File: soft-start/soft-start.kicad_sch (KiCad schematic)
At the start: 17 parts

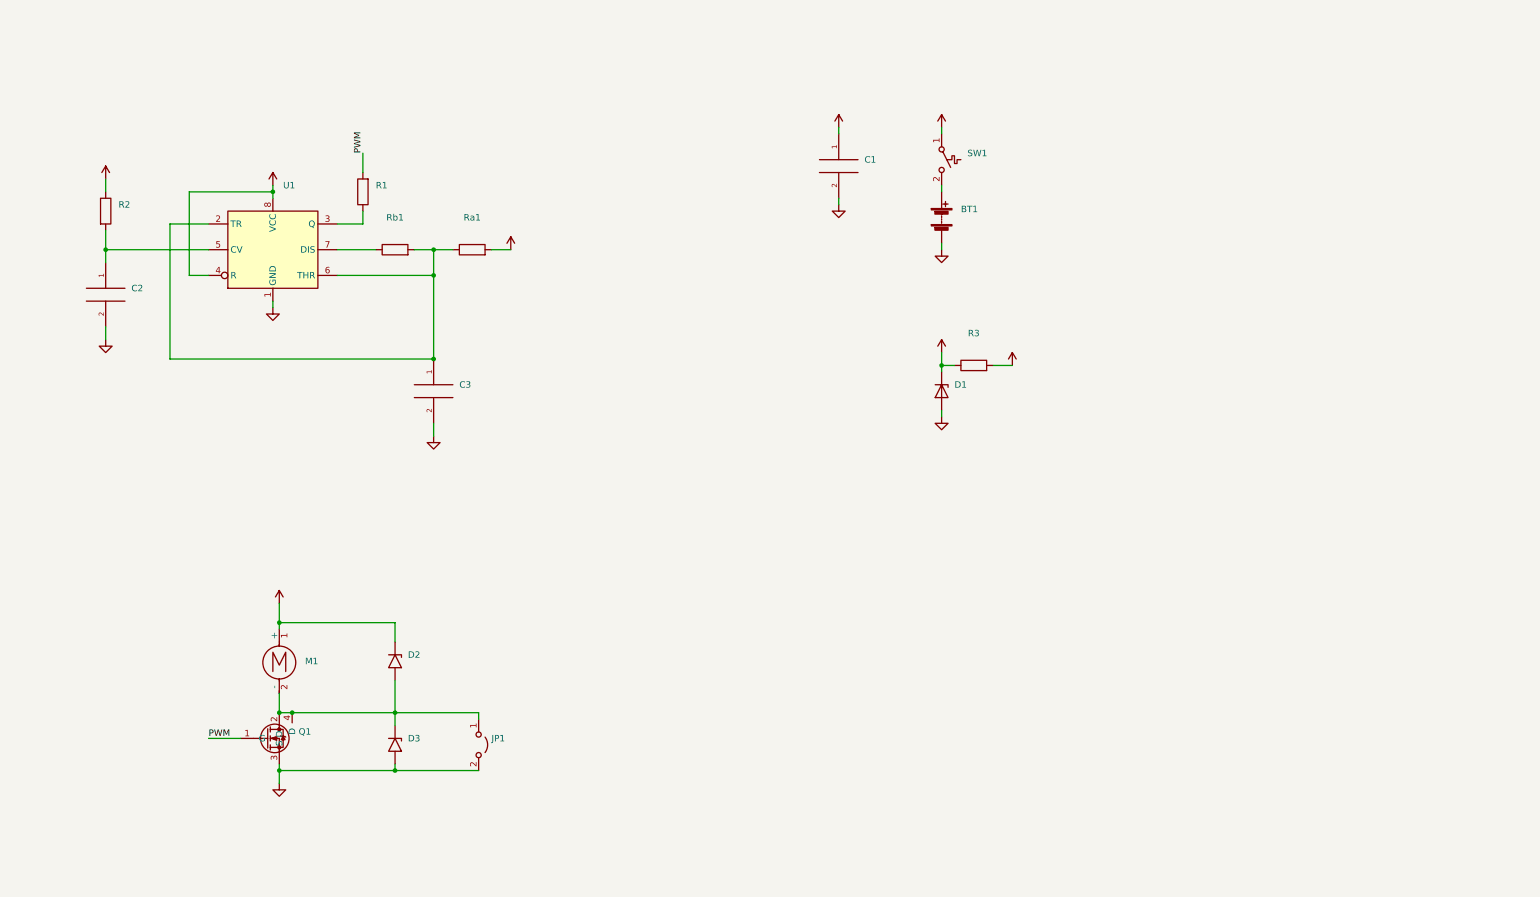
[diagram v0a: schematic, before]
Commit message: [soft-start] Add power supply
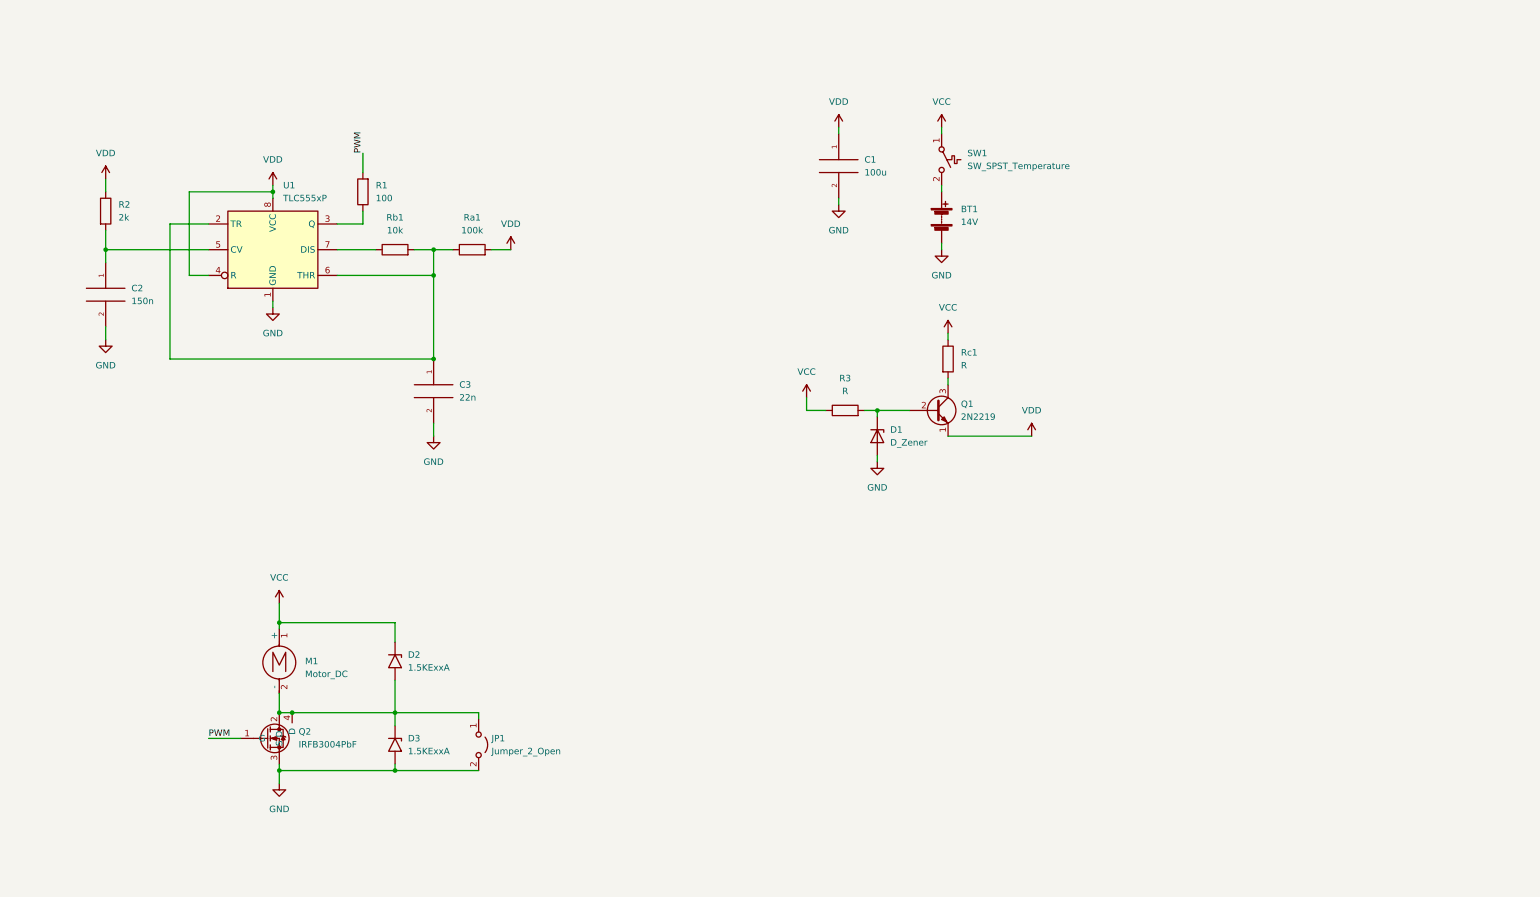
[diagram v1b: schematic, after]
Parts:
- added Q1: 2N2219, Package_TO_SOT_THT:TO-39-3, symbol Transistor_BJT:2N2219
- added Rc1: R, symbol Device:R
- BT1: value (none) -> 14V; footprint (none) -> Battery:BatteryHolder_Bulgin_BX0036_1xC
- C1: value (none) -> 100u; footprint (none) -> Capacitor_THT:C_Axial_L5.1mm_D3.1mm_P7.50mm_Horizontal
- C2: value (none) -> 150n; footprint (none) -> Capacitor_THT:C_Axial_L5.1mm_D3.1mm_P7.50mm_Horizontal
- C3: value (none) -> 22n; footprint (none) -> Capacitor_THT:C_Axial_L5.1mm_D3.1mm_P7.50mm_Horizontal
- D1: value (none) -> D_Zener; footprint (none) -> Diode_THT:D_DO-15_P3.81mm_Vertical_AnodeUp
- D2, D3: value (none) -> 1.5KExxA; footprint (none) -> Diode_THT:D_DO-201AE_P15.24mm_Horizontal
- JP1: value (none) -> Jumper_2_Open; footprint (none) -> Connector_Wire:SolderWire-2sqmm_1x03_P7.8mm_D2mm_OD3.9mm_Relief2x
- M1: value (none) -> Motor_DC; footprint (none) -> Connector_Wire:SolderWire-2sqmm_1x03_P7.8mm_D2mm_OD3.9mm_Relief2x
- Q2: renamed from Q1; value (none) -> IRFB3004PbF; footprint (none) -> LIB:TO-220-3-4_Horizontal_TabDown
- R1: value (none) -> 100; footprint (none) -> Resistor_THT:R_Axial_DIN0207_L6.3mm_D2.5mm_P2.54mm_Vertical
- R2: value (none) -> 2k; footprint (none) -> Resistor_THT:R_Axial_DIN0207_L6.3mm_D2.5mm_P5.08mm_Vertical
- R3: value (none) -> R; footprint (none) -> Resistor_THT:R_Axial_DIN0207_L6.3mm_D2.5mm_P5.08mm_Vertical
- Ra1: value (none) -> 100k; footprint (none) -> Resistor_THT:R_Axial_DIN0207_L6.3mm_D2.5mm_P5.08mm_Vertical
- Rb1: value (none) -> 10k; footprint (none) -> Resistor_THT:R_Axial_DIN0207_L6.3mm_D2.5mm_P5.08mm_Vertical
- SW1: value (none) -> SW_SPST_Temperature; footprint (none) -> Connector_Wire:SolderWire-2sqmm_1x02_P7.8mm_D2mm_OD3.9mm_Relief2x
- U1: value (none) -> TLC555xP; footprint (none) -> Package_DIP:DIP-8_W7.62mm
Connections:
- net VCC: now also Rc1.1; no longer D1.1 (K)
- net VDD: now also Q1.1 (E); no longer R3.2
- new net: D1.1 (K), Q1.2 (B), R3.2
- new net: Q1.3 (C), Rc1.2
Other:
- moved on the sheet: D1, R3

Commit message: [soft-start] Add PCB
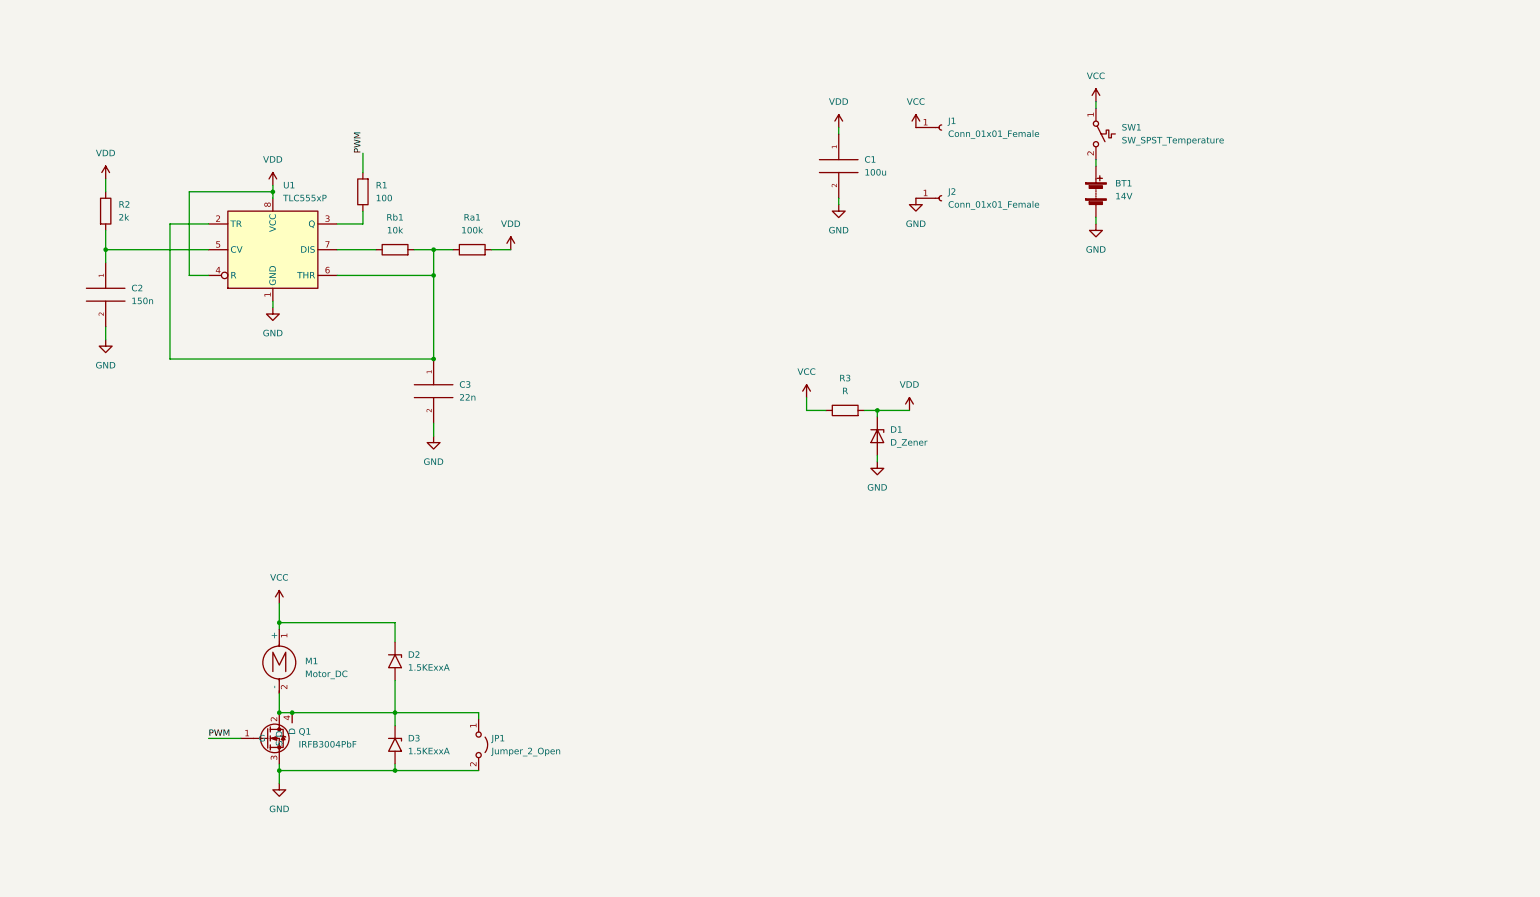
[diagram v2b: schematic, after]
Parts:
- removed Q1: 2N2219, Package_TO_SOT_THT:TO-39-3, symbol Transistor_BJT:2N2219
- removed Rc1: R, symbol Device:R
- added J1, J2: Conn_01x01_Female, Connector_Wire:SolderWire-2.5sqmm_1x01_D2.4mm_OD3.6mm, symbol Connector:Conn_01x01_Female
- BT1: footprint Battery:BatteryHolder_Bulgin_BX0036_1xC -> Connector_Wire:SolderWire-2.5sqmm_1x02_P8.8mm_D2.4mm_OD4.4mm
- D1: footprint Diode_THT:D_DO-15_P3.81mm_Vertical_AnodeUp -> Diode_THT:D_DO-41_SOD81_P3.81mm_Vertical_AnodeUp
- JP1, M1: footprint Connector_Wire:SolderWire-2sqmm_1x03_P7.8mm_D2mm_OD3.9mm_Relief2x -> Connector_Wire:SolderWire-2.5sqmm_1x02_P8.8mm_D2.4mm_OD4.4mm
- R1: footprint Resistor_THT:R_Axial_DIN0207_L6.3mm_D2.5mm_P2.54mm_Vertical -> Resistor_THT:R_Axial_DIN0207_L6.3mm_D2.5mm_P15.24mm_Horizontal
- SW1: footprint Connector_Wire:SolderWire-2sqmm_1x02_P7.8mm_D2mm_OD3.9mm_Relief2x -> Connector_Wire:SolderWire-2.5sqmm_1x02_P8.8mm_D2.4mm_OD4.4mm
- renumbered Q2 to Q1
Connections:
- net GND: now also J2.1 (Pin_1)
- net VCC: now also J1.1 (Pin_1)
- net VDD: now also D1.1 (K), R3.2
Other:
- moved on the sheet: BT1, SW1

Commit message: [soft-start] Update to use counter as time delay source
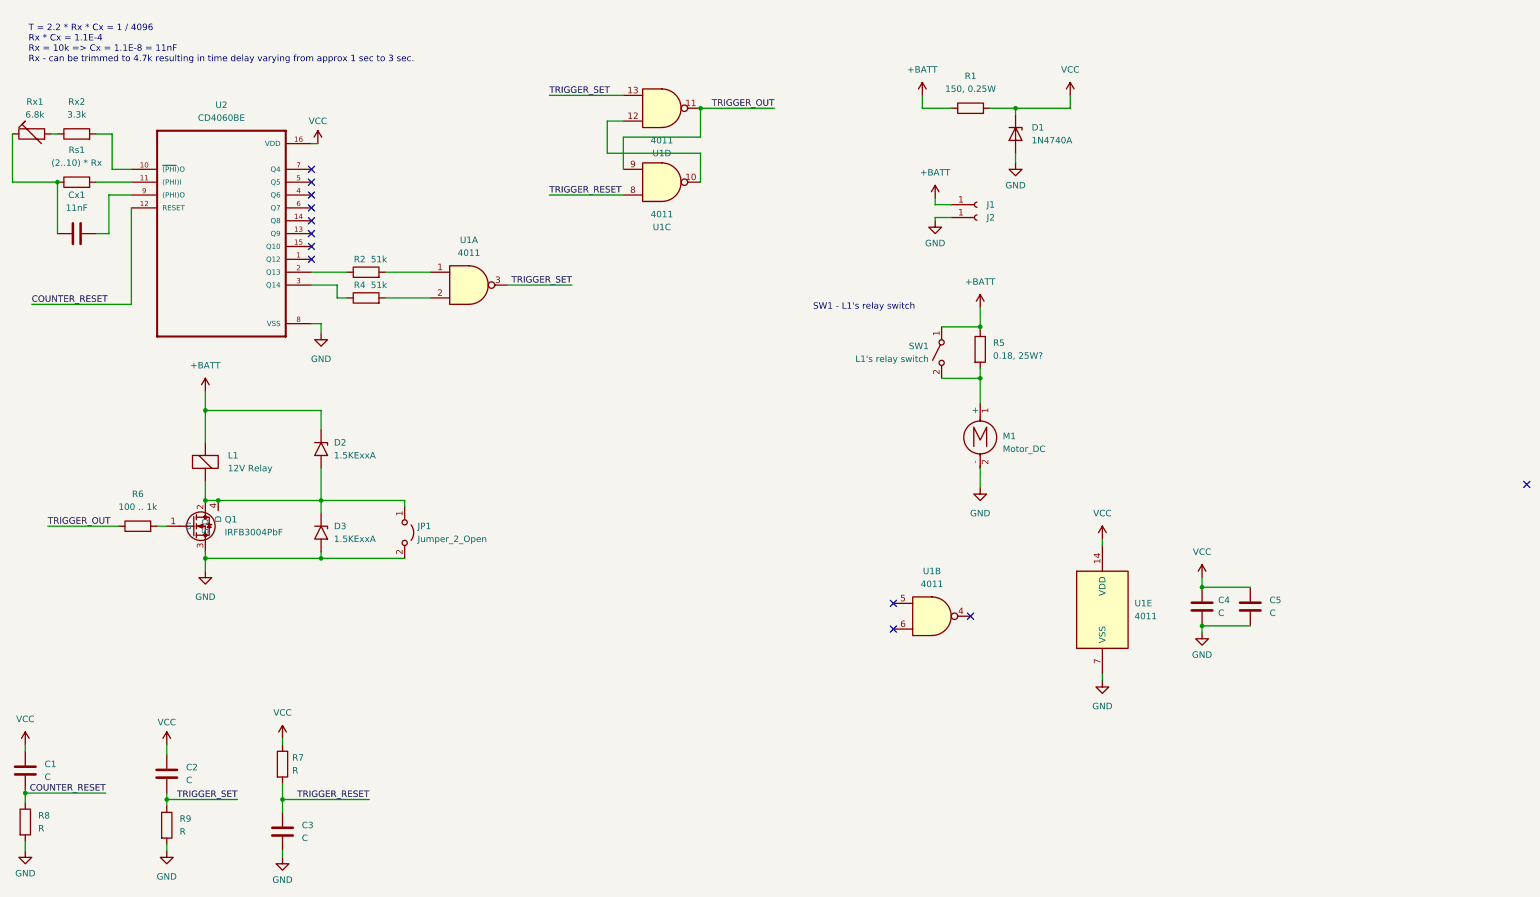
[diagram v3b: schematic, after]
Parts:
- removed BT1: 14V, Connector_Wire:SolderWire-2.5sqmm_1x02_P8.8mm_D2.4mm_OD4.4mm, symbol Device:Battery
- removed C1: 100u, Capacitor_THT:C_Axial_L5.1mm_D3.1mm_P7.50mm_Horizontal, symbol pspice:C
- removed C2: 150n, Capacitor_THT:C_Axial_L5.1mm_D3.1mm_P7.50mm_Horizontal, symbol pspice:C
- removed C3: 22n, Capacitor_THT:C_Axial_L5.1mm_D3.1mm_P7.50mm_Horizontal, symbol pspice:C
- removed D1: D_Zener, Diode_THT:D_DO-41_SOD81_P3.81mm_Vertical_AnodeUp, symbol Device:D_Zener
- removed J1, J2: Conn_01x01_Female, Connector_Wire:SolderWire-2.5sqmm_1x01_D2.4mm_OD3.6mm, symbol Connector:Conn_01x01_Female
- removed R3: R, Resistor_THT:R_Axial_DIN0207_L6.3mm_D2.5mm_P5.08mm_Vertical, symbol Device:R
- removed Ra1: 100k, Resistor_THT:R_Axial_DIN0207_L6.3mm_D2.5mm_P5.08mm_Vertical, symbol Device:R
- removed Rb1: 10k, Resistor_THT:R_Axial_DIN0207_L6.3mm_D2.5mm_P5.08mm_Vertical, symbol Device:R
- removed SW1: SW_SPST_Temperature, Connector_Wire:SolderWire-2.5sqmm_1x02_P8.8mm_D2.4mm_OD4.4mm, symbol Switch:SW_SPST_Temperature
- removed U1: TLC555xP, Package_DIP:DIP-8_W7.62mm, symbol Timer:TLC555xP
- added C1, C2, C3, C4, C5: C, Capacitor_THT:C_Disc_D6.0mm_W4.4mm_P5.00mm, symbol Device:C
- added Cx1: 11nF, Capacitor_THT:C_Disc_D6.0mm_W4.4mm_P5.00mm, symbol Device:C
- added D1: 1N4740A, Diode_THT:D_DO-41_SOD81_P10.16mm_Horizontal, symbol Diode:1N47xxA
- added J1, J2: ~, Connector_Wire:SolderWire-2.5sqmm_1x01_D2.4mm_OD3.6mm, symbol Connector:Conn_01x01_Socket
- added L1: 12V Relay, symbol Device:ElectromagneticActor
- added R4: 51k, Resistor_THT:R_Axial_DIN0207_L6.3mm_D2.5mm_P2.54mm_Vertical, symbol Device:R
- added R5: 0.18, 25W?, Connector_Wire:SolderWire-2.5sqmm_1x02_P7.2mm_D2.4mm_OD3.6mm, symbol Device:R
- added R6: 100 .. 1k, Resistor_THT:R_Axial_DIN0207_L6.3mm_D2.5mm_P2.54mm_Vertical, symbol Device:R
- added R7, R8, R9: R, Resistor_THT:R_Axial_DIN0207_L6.3mm_D2.5mm_P2.54mm_Vertical, symbol Device:R
- added Rs1: (2..10) * Rx, Resistor_THT:R_Axial_DIN0207_L6.3mm_D2.5mm_P2.54mm_Vertical, symbol Device:R
- added Rx1: 6.8k, Resistor_THT:R_Axial_DIN0207_L6.3mm_D2.5mm_P7.62mm_Horizontal, symbol Device:R_Trim
- added Rx2: 3.3k, Resistor_THT:R_Axial_DIN0207_L6.3mm_D2.5mm_P2.54mm_Vertical, symbol Device:R
- added SW1: L1's relay switch, symbol Switch:SW_SPST
- added U1: 4011, Package_DIP:DIP-14_W7.62mm_Socket_LongPads, symbol 4xxx:4011
- added U2: CD4060BE, DIP794W45P254L1969H508Q16, symbol CD4060BE:CD4060BE
- JP1: footprint Connector_Wire:SolderWire-2.5sqmm_1x02_P8.8mm_D2.4mm_OD4.4mm -> Connector_Wire:SolderWire-1.5sqmm_1x02_P7.8mm_D1.7mm_OD3.9mm
- M1: footprint Connector_Wire:SolderWire-2.5sqmm_1x02_P8.8mm_D2.4mm_OD4.4mm -> (none); now left out of the parts list
- R1: value 100 -> 150, 0.25W; footprint Resistor_THT:R_Axial_DIN0207_L6.3mm_D2.5mm_P15.24mm_Horizontal -> Resistor_THT:R_Axial_DIN0207_L6.3mm_D2.5mm_P2.54mm_Vertical
- R2: value 2k -> 51k; footprint Resistor_THT:R_Axial_DIN0207_L6.3mm_D2.5mm_P5.08mm_Vertical -> Resistor_THT:R_Axial_DIN0207_L6.3mm_D2.5mm_P2.54mm_Vertical
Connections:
- net GND: now also M1.2 (-), C3.2, C4.2, C5.2, D1.2 (A), J2.1 (Pin_1), R8.2, R9.2, U1.7 (VSS), U2.8 (VSS)
- net VCC: now also R1.2, C1.1, C2.1, C4.1, C5.1, D1.1 (K), R7.1, U1.14 (VDD), U2.16 (VDD); no longer D2.1 (A1), M1.1 (+)
- net at D2.2 (A2), D3.1 (A1), JP1.1 (A)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: now also L1.2 (+); no longer M1.2 (-)
- net +BATT: now reaches R1.1
- net +BATT: now also D2.1 (A1), J1.1 (Pin_1), L1.1 (-), R5.1, SW1.1 (A)
- net at R2.2: now also U1.1
- net PWM: no longer names the net of Q1.1 (G)
- net PWM: now also R6.2; no longer R1.2
- net VDD: no longer names the net of R2.1
- net VDD: now also U2.2 (Q13)
- new net: Rx2.2, U2.10 (~{(PHI})O~{})
- new net: Rs1.2, U2.11 ((PHI)I)
- new net: R4.1, U2.3 (Q14)
- new net: Cx1.2, U2.9 ((PHI)O)
- new net: Cx1.1, Rs1.1, Rx1.1
- new net: U1.10, U1.12
- new net: M1.1 (+), R5.2, SW1.2 (B)
- new net: R4.2, U1.2
- new net: Rx1.2, Rx2.1
- new net COUNTER_RESET: C1.2, R8.1, U2.12 (RESET)
- new net TRIGGER_OUT: R6.1, U1.11, U1.9
- new net TRIGGER_RESET: C3.1, R7.2, U1.8
- new net TRIGGER_SET: C2.2, R9.1, U1.13, U1.3
- no-connect marks 0 -> 12
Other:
- note added: "SW1 - L1's relay switch"
- note added: "T = 2.2 * Rx * Cx = 1 / 4096 Rx * Cx = 1.1E-4 Rx = 10k => Cx = 1.1E-8 = 11nF Rx - can be trimmed to 4.7k resulting in time delay varying from approx 1 sec to 3 sec."
- moved on the sheet: D2, D3, JP1, Q1
